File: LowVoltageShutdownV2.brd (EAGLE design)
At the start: 23.8 x 21 mm, 7 parts

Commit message: second revision and added 3D models
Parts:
- removed BAT+, GND: 16G, Wire2Board:16G
- removed U$2: SISS23DN-T1-GE3CY-ND, SISS23DN-T1-GE3CT-ND:POWERPAK1212-8S
- added Q1: FDD4141TO252, transistor-fet:TO252
- added U$5, U$6: 450PAD, Wire2Board:450PAD
- moved U$3 38.9 mm to (14.0, 44.5), turned to 180 degrees
- moved U$1 26.7 mm to (12.7, 33.0), flipped to the bottom
- moved OUT 21.4 mm to (-2.54, 19.1), turned to 270 degrees
- moved U$4 6.55 mm to (5.08, 17.8), turned to 300 degrees
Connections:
- removed net BAT+: BAT+.P$1, U$1.5, U$2.S, U$3.P$1
- new net BAT: Q1.2, U$1.5, U$3.P$1, U$5.P$1
- net GND: now also U$6.P$1; no longer GND.P$1
- net N$5: now also Q1.1; no longer U$2.G
- net OUT: now also Q1.3; no longer U$2.D
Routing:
- net BAT: track 0.00 -> 23.2 mm, vias 0 -> 1
- net BAT+: track 21.4 -> 0.00 mm
- net N$5: track 4.10 -> 19.3 mm, vias 0 -> 1
- net GND: track 23.7 -> 36.9 mm
- net OUT: track 10.6 -> 0.00 mm
- net N$1: track 5.97 -> 13.5 mm
- added copper zone on layer 1, net BAT
- added copper zone on layer 1, net OUT
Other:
- board size 23.8 x 21 mm -> 22.9 x 63.5 mm

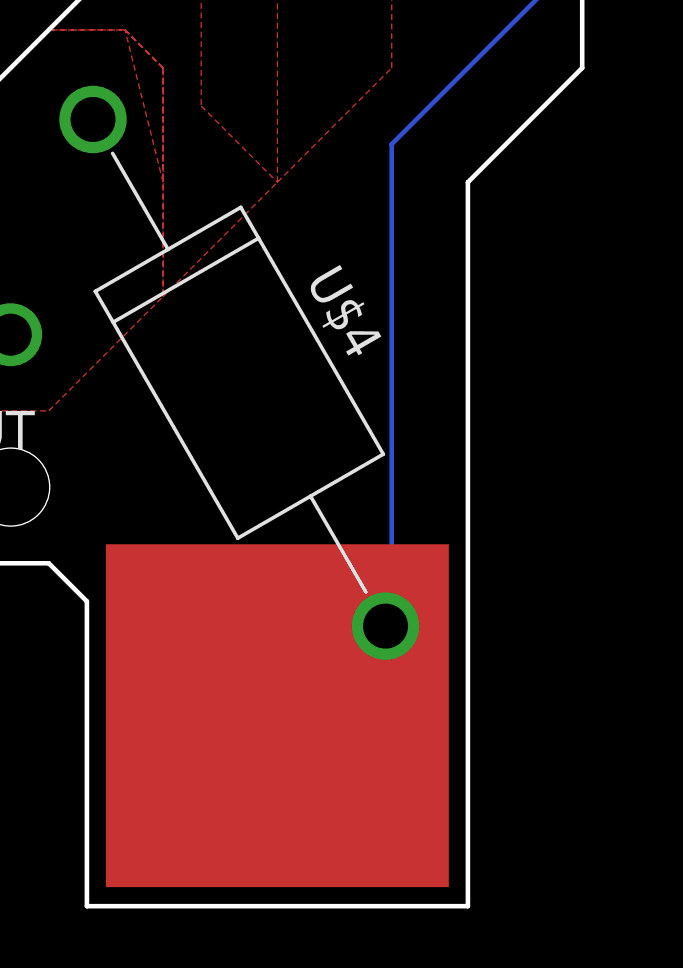
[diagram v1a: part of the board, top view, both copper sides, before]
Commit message: added ground pin
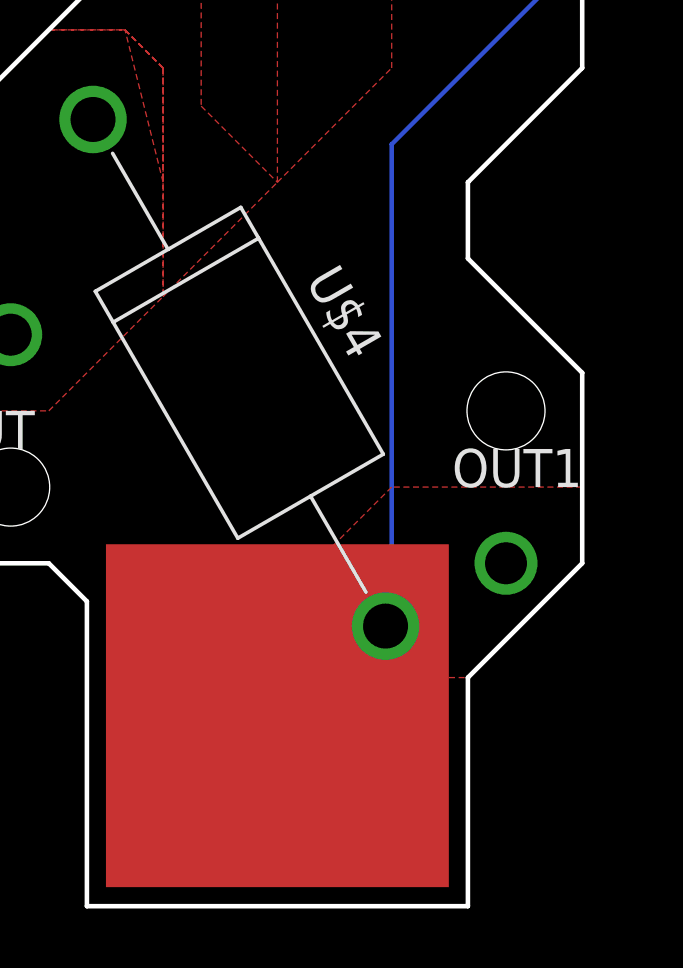
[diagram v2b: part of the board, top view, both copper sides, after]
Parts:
- added OUT1: 16G, Wire2Board:16G
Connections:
- net GND: now also OUT1.P$1
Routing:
- added copper zone on layer 1, net GND
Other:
- outline, holes or cut-outs redrawn
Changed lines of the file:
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@@
 <?xml version="1.0" encoding="utf-8"?>
 <!DOCTYPE eagle SYSTEM "eagle.dtd">
-<eagle version="9.0.0">
+<eagle version="9.0.1">
 <drawing>
 <settings>
@@
 </layers>
 <board>
-<fusionsync huburn="a.cGVyc29uYWw6dWUyYjU3ZGRj" projecturn="a.cGVyc29uYWw6dWUyYjU3ZGRjIzIwMTgwNDIwMTI4NTIzNDI2" f3durn="urn:adsk.wipprod:dm.lineage:2b7arQ8oTve2K50kV5ObSw" pcbguid="f91a00e0-6f1a-40d0-9885-178f57955412" lastpulledtime="" lastsyncedchangeguid="2c076a4a-38ea-13a7-c86a-f221a3de4af9"/>
+<fusionsync huburn="a.cGVyc29uYWw6dWUyYjU3ZGRj" projecturn="a.cGVyc29uYWw6dWUyYjU3ZGRjIzIwMTgwNDIwMTI4NTIzNDI2" f3durn="urn:adsk.wipprod:dm.lineage:2b7arQ8oTve2K50kV5ObSw" pcbguid="f91a00e0-6f1a-40d0-9885-178f57955412" lastpulledtime="" lastsyncedchangeguid="e0ff1466-a955-48c7-1103-8f0f917de349"/>
 <plain>
-<wire x1="12.7" y1="0" x2="12.7" y2="24.13" width="0.1524" layer="20"/>
+<wire x1="12.7" y1="0" x2="12.7" y2="7.62" width="0.1524" layer="20"/>
+<wire x1="12.7" y1="21.59" x2="12.7" y2="24.13" width="0.1524" layer="20"/>
 <wire x1="12.7" y1="52.07" x2="12.7" y2="63.5" width="0.1524" layer="20"/>
 <wire x1="12.7" y1="63.5" x2="0" y2="63.5" width="0.1524" layer="20"/>
@@
 <wire x1="17.78" y1="38.1" x2="16.51" y2="36.83" width="0.1524" layer="20"/>
 <wire x1="16.51" y1="36.83" x2="16.51" y2="27.94" width="0.1524" layer="20"/>
+<wire x1="12.7" y1="7.62" x2="16.51" y2="11.43" width="0.1524" layer="20"/>
+<wire x1="16.51" y1="11.43" x2="16.51" y2="17.78" width="0.1524" layer="20"/>
+<wire x1="16.51" y1="17.78" x2="12.7" y2="21.59" width="0.1524" layer="20"/>
 </plain>
 <attributes>
@@
 <element name="U$6" library="Wire2Board" package="450PAD" package3d_urn="urn:adsk.eagle:package:3080342/2" value="450PAD" x="6.35" y="6.35"/>
 <element name="Q1" library="transistor-fet" library_urn="urn:adsk.eagle:library:396" package="TO252" package3d_urn="urn:adsk.eagle:package:28537/2" value="FDD4141TO252" x="5.08" y="36.83" rot="R180"/>
+<element name="OUT1" library="Wire2Board" package="16G" package3d_urn="urn:adsk.eagle:package:3080160/3" value="16G" x="13.97" y="11.43" rot="R90"/>
 </elements>
 <signals>
@@
 <wire x1="10.16" y1="25.4" x2="15.24" y2="30.48" width="0.1524" layer="16"/>
 <wire x1="15.24" y1="30.48" x2="15.24" y2="33.02" width="0.1524" layer="16"/>
-<wire x1="6.35" y1="6.35" x2="9.955" y2="9.33625" width="0" layer="19" extent="1-1"/>
+<contactref element="OUT1" pad="P$1"/>
+<polygon width="0.1524" layer="1" thermals="no">
+<vertex x="11.43" y="7.62"/>
+<vertex x="12.7" y="7.62"/>
+<vertex x="16.51" y="11.43"/>
+<vertex x="16.51" y="13.97"/>
+<vertex x="10.16" y="13.97"/>
+<vertex x="7.62" y="11.43"/>
+<vertex x="7.62" y="8.89"/>
+<vertex x="8.89" y="7.62"/>
+</polygon>
+<wire x1="9.955" y1="9.33625" x2="6.35" y2="6.35" width="0" layer="19" extent="1-1"/>
 </signal>
 <signal name="BAT">
